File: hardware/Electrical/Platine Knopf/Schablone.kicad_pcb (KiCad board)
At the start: 2 copper layers, 23.5 x 23.5 mm, 2 parts, among them J1 Conn_01x05_Pin, U1 49E

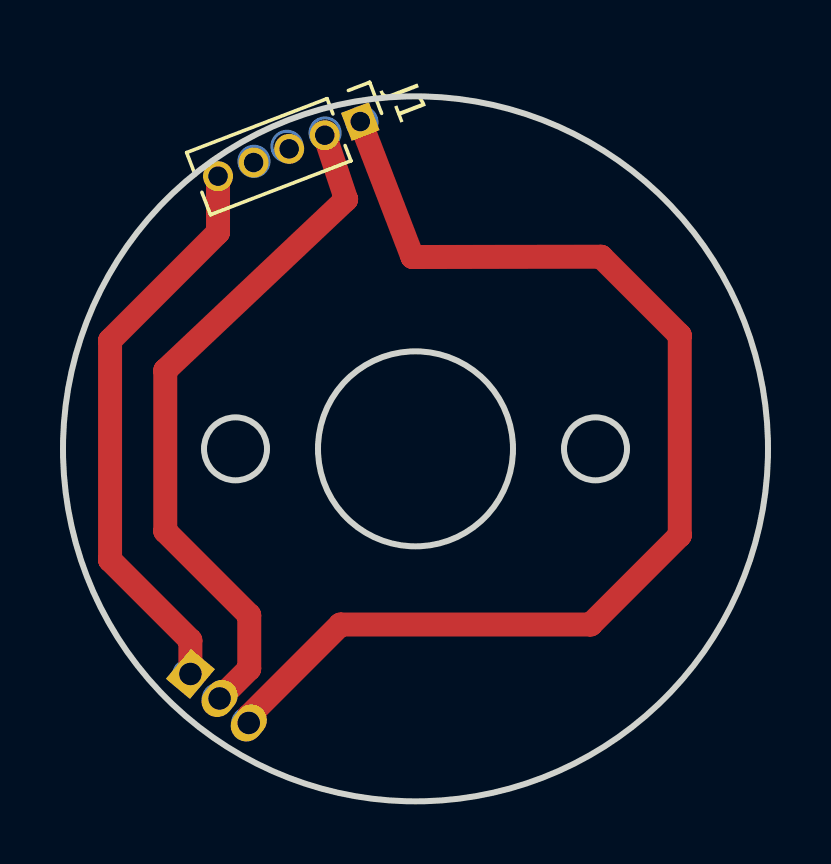
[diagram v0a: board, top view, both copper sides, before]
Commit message: Platinen optimiert
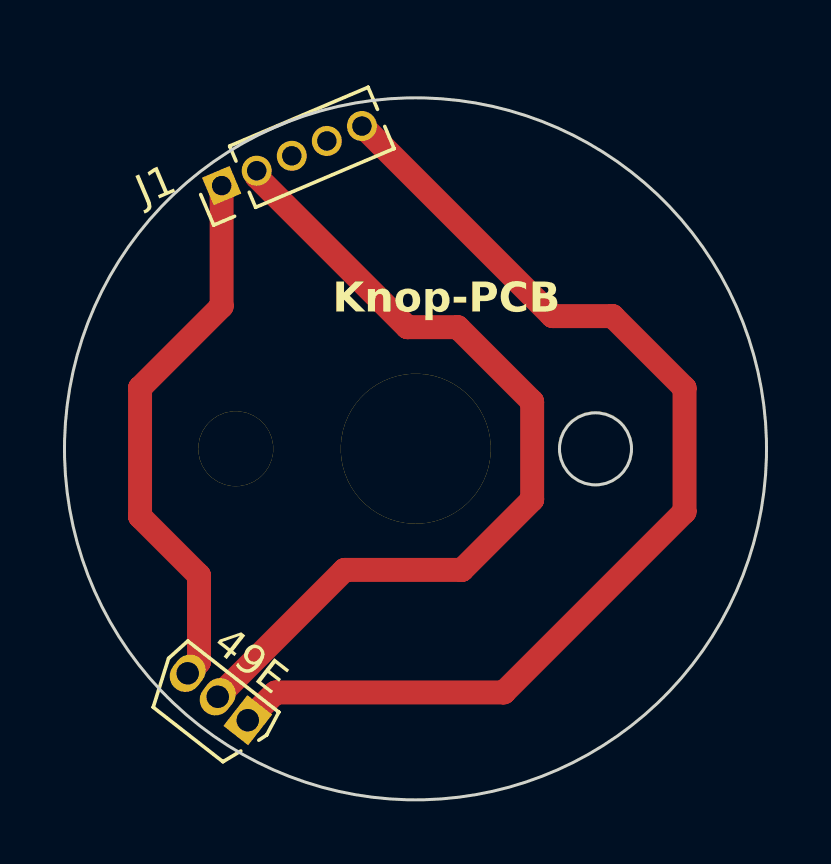
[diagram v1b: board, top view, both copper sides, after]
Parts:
- added REF**: MountingHole_2.5mm, MountingHole:MountingHole_2.5mm, F.Cu at (152.0, 90.2)
- added REF**: MountingHole_5mm, MountingHole:MountingHole_5mm, F.Cu at (146.0, 90.2)
- added REF**: MountingHole_2.5mm, MountingHole:MountingHole_2.5mm, F.Cu at (140.0, 90.2)
- U1: moved to F.Cu
- moved J1 5.09 mm to (139.5, 81.5), turned to 113 degrees
- moved U1 2.46 mm to (140.4, 99.3), turned to 142 degrees
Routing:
- net Net-(J1-Pin_1): track 38.6 -> 18.4 mm
- net Net-(J1-Pin_5): track 19.2 -> 36.2 mm
- net Net-(J1-Pin_2): track 23.1 -> 29.0 mm
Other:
- board size 23.5 x 23.5 mm -> 23.4 x 23.4 mm
- board text added: "AFUDirk"
- board text added: "GND"
- board text added: "Knop-PCB"
- board text added: "Rotate"
- board text added: "Touch"
- board text added: "V+"
- board text added: "Zoom"
